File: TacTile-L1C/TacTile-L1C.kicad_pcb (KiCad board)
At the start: 2 copper layers, 25 x 25 mm, 2 parts, among them J1 Conn_01x02, J2 Conn_01x02

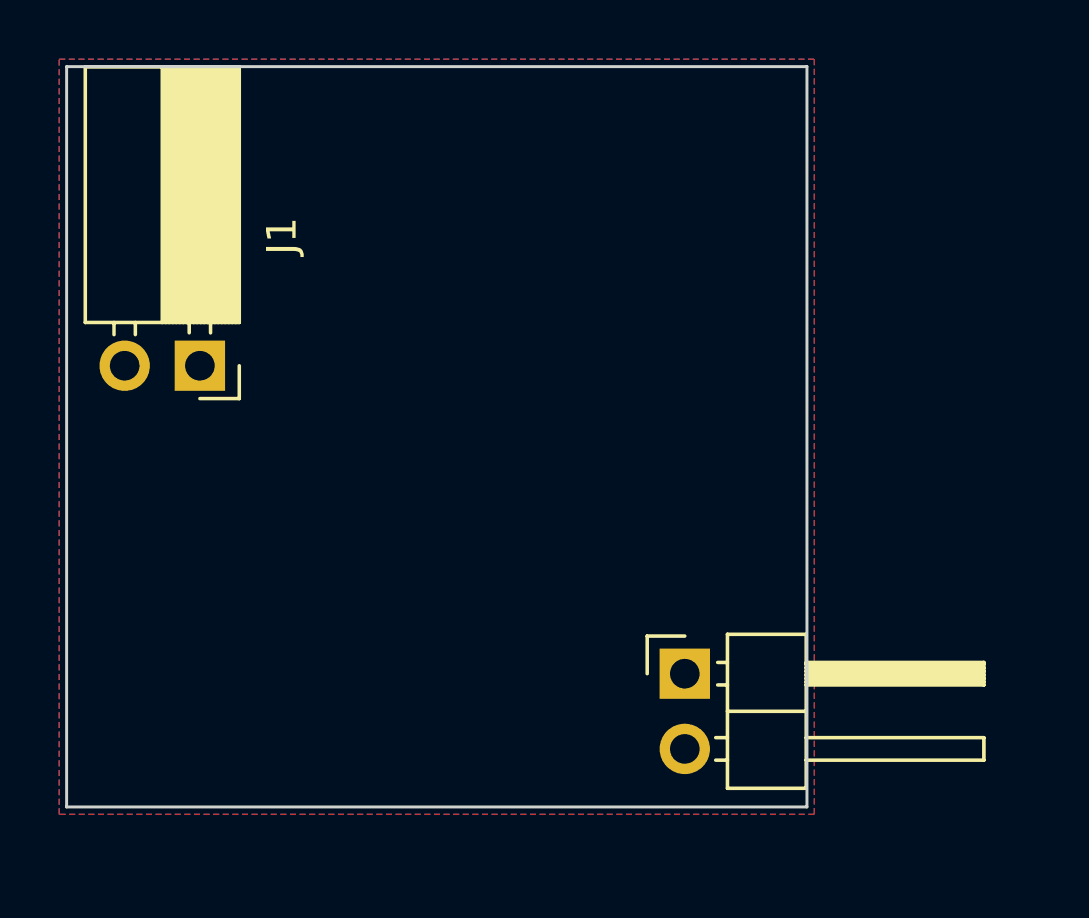
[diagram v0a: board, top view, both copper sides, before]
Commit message: Adjusted mounting for laser boards
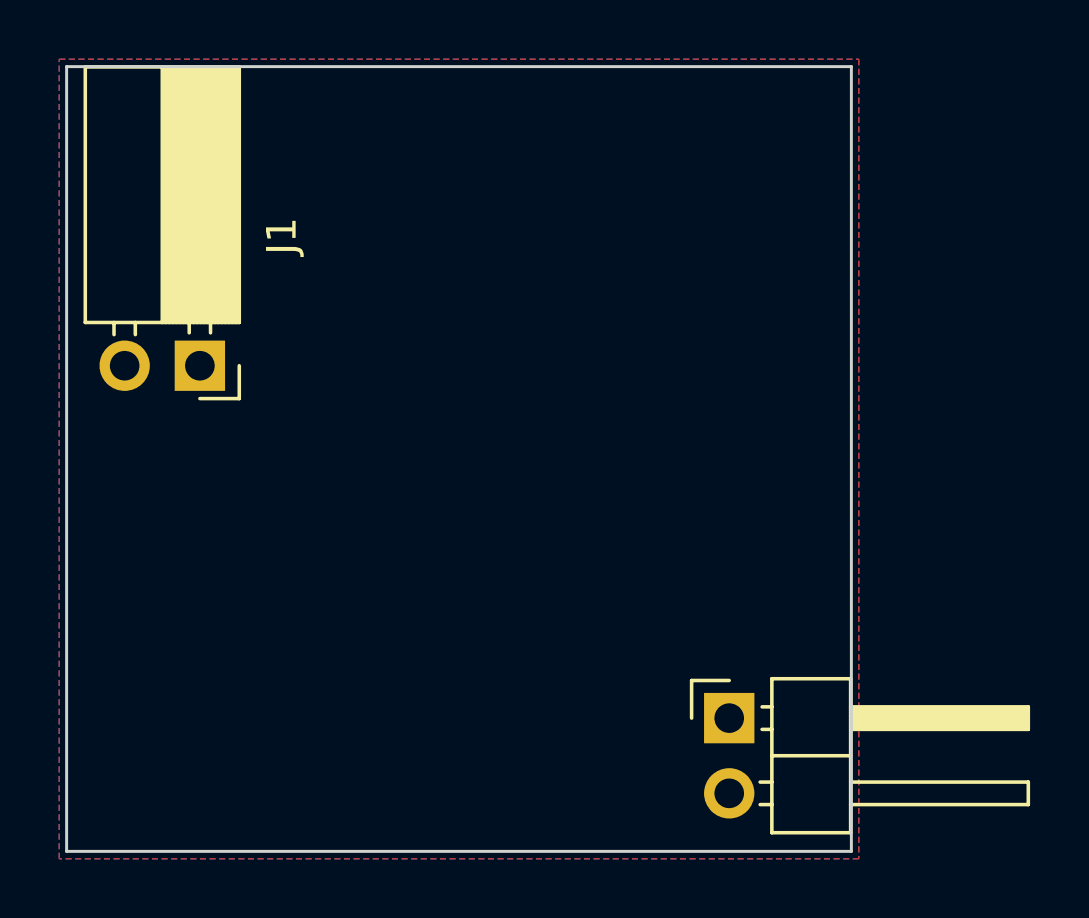
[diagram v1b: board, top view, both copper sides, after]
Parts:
- moved J2 2.12 mm to (47.4, 47.0)
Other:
- board size 25 x 25 mm -> 26.5 x 26.5 mm
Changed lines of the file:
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@@
   (net 2 "/GND")
   (footprint "Connector_PinHeader_2.54mm:PinHeader_1x02_P2.54mm_Horizontal" (layer "F.Cu")
-    (at 45.875 45.5)
+    (at 47.375 47)
     (descr "Through hole angled pin header, 1x02, 2.54mm pitch, 6mm pin length, single row")
     (tags "Through hole angled pin header THT 1x02 2.54mm single row")
@@
     )
   )
-  (gr_rect (start 25 25) (end 50 50)
+  (gr_rect (start 25 25) (end 51.5 51.5)
     (stroke (width 0.1) (type default)) (fill none) (layer "Edge.Cuts"))
   (zone (net 1) (net_name "/VCC") (layer "F.Cu") (hatch edge 0.5)
@@
       (pts
         (xy 24.75 24.75)
-        (xy 50.25 24.75)
-        (xy 50.25 50.25)
-        (xy 24.75 50.25)
+        (xy 51.75 24.75)
+        (xy 51.75 51.75)
+        (xy 24.75 51.75)
       )
     )
@@
       (pts
         (xy 24.75 24.75)
-        (xy 50.25 24.75)
-        (xy 50.25 50.25)
-        (xy 24.75 50.25)
+        (xy 51.75 24.75)
+        (xy 51.75 51.75)
+        (xy 24.75 51.75)
       )
     )
